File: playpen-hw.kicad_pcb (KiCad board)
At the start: 2 copper layers, 63.5 x 48.5 mm, 2 parts, among them J1 USB_C_Receptacle_USB2.0_16P, U2 STM32G473CEUx

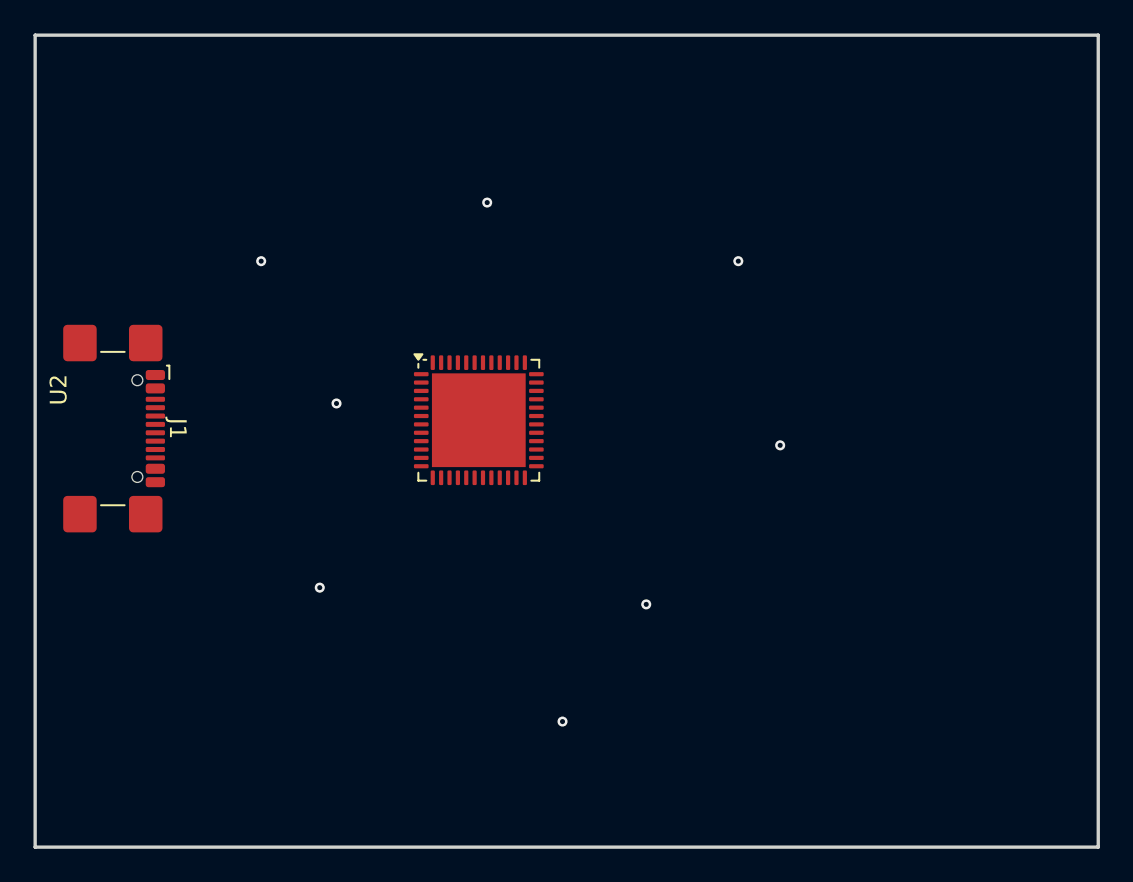
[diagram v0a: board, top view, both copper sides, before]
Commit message: Testing KiCAD CI job (#2)
* Testing KiCAD CI job

* Splitting into multiple workflows for scalability

* Naming workflows better names
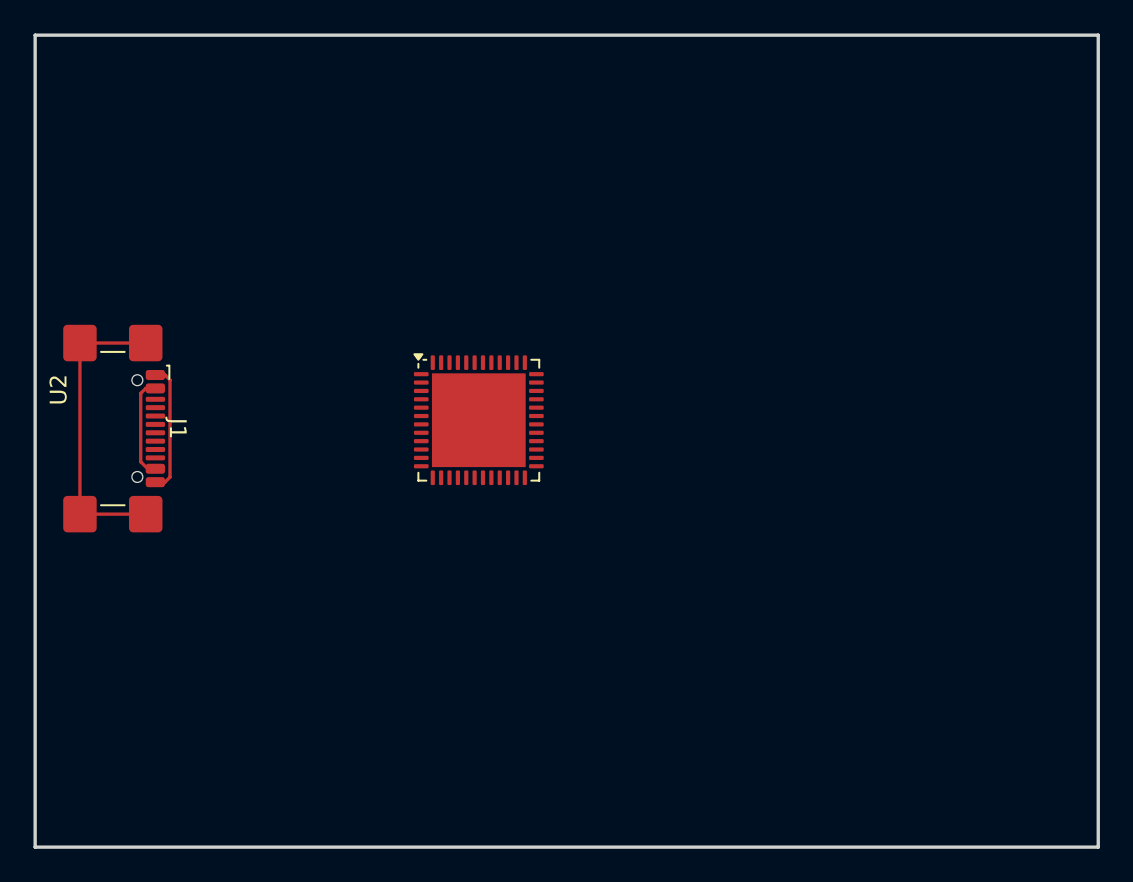
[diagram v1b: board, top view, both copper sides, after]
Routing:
- net unconnected-(J1-SHIELD-PadS1): track 0.00 -> 18.1 mm
- net Net-(J1-GND-PadA1): track 0.00 -> 7.80 mm
- net Net-(J1-VBUS-PadA4): track 0.00 -> 6.13 mm
- net (no net): vias 8 -> 0
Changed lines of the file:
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@@
 		(layer "Edge.Cuts")
 	)
-	(via
-		(at 165.5 101.5)
-		(size 0.6)
-		(drill 0.3)
-		(layers "F.Cu" "B.Cu")
-		(net 0)
+	(segment
+		(start 123.675 95.39)
+		(end 127.605 95.39)
+		(width 0.2)
+		(layer "F.Cu")
+		(net 1)
 	)
-	(via
-		(at 163 90.5)
-		(size 0.6)
-		(drill 0.3)
-		(layers "F.Cu" "B.Cu")
-		(net 0)
+	(segment
+		(start 123.675 105.61)
+		(end 127.605 105.61)
+		(width 0.2)
+		(layer "F.Cu")
+		(net 1)
 	)
-	(via
-		(at 134.5 90.5)
-		(size 0.6)
-		(drill 0.3)
-		(layers "F.Cu" "B.Cu")
-		(net 0)
+	(segment
+		(start 123.675 105.61)
+		(end 123.675 95.39)
+		(width 0.2)
+		(layer "F.Cu")
+		(net 1)
 	)
-	(via
-		(at 148 87)
-		(size 0.6)
-		(drill 0.3)
-		(layers "F.Cu" "B.Cu")
-		(net 0)
+	(segment
+		(start 128.18 98.1)
+		(end 127.605001 98.1)
+		(width 0.2)
+		(layer "F.Cu")
+		(net 2)
 	)
-	(via
-		(at 157.5 111)
-		(size 0.6)
-		(drill 0.3)
-		(layers "F.Cu" "B.Cu")
-		(net 0)
+	(segment
+		(start 127.305 102.48241)
+		(end 127.72259 102.9)
+		(width 0.2)
+		(layer "F.Cu")
+		(net 2)
 	)
-	(via
-		(at 152.5 118)
-		(size 0.6)
-		(drill 0.3)
-		(layers "F.Cu" "B.Cu")
-		(net 0)
+	(segment
+		(start 127.72259 102.9)
+		(end 128.18 102.9)
+		(width 0.2)
+		(layer "F.Cu")
+		(net 2)
 	)
-	(via
-		(at 139 99)
-		(size 0.6)
-		(drill 0.3)
-		(layers "F.Cu" "B.Cu")
-		(net 0)
+	(segment
+		(start 127.605001 98.1)
+		(end 127.305 98.400001)
+		(width 0.2)
+		(layer "F.Cu")
+		(net 2)
 	)
-	(via
-		(at 138 110)
-		(size 0.6)
-		(drill 0.3)
-		(layers "F.Cu" "B.Cu")
-		(net 0)
+	(segment
+		(start 127.305 98.400001)
+		(end 127.305 102.48241)
+		(width 0.2)
+		(layer "F.Cu")
+		(net 2)
+	)
+	(segment
+		(start 128.754999 97.3)
+		(end 129.055 97.600001)
+		(width 0.2)
+		(layer "F.Cu")
+		(net 6)
+	)
+	(segment
+		(start 129.055 97.600001)
+		(end 129.055 103.399999)
+		(width 0.2)
+		(layer "F.Cu")
+		(net 6)
+	)
+	(segment
+		(start 129.055 103.399999)
+		(end 128.754999 103.7)
+		(width 0.2)
+		(layer "F.Cu")
+		(net 6)
+	)
+	(segment
+		(start 128.754999 103.7)
+		(end 128.18 103.7)
+		(width 0.2)
+		(layer "F.Cu")
+		(net 6)
+	)
+	(segment
+		(start 128.18 97.3)
+		(end 128.754999 97.3)
+		(width 0.2)
+		(layer "F.Cu")
+		(net 6)
 	)
 )
